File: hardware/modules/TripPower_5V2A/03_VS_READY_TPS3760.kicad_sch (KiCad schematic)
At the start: 13 parts, among them Q303 BVSS123LT1G 100V AEC-Q101, U302 TPS3760A012DYYRQ1

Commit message: feat(TripPower): replace leaking EN source follower with VS-only 300V automotive PNP/NPN gated high-side drive; isolate RUN and AUTO
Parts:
- removed D306: BAS70-02V-HG3-08 GATE TO RESET SCHOTTKY, Diode_SMD:D_SOD-523, symbol TripPower_Sym:BAS70_02V_A1_K2
- removed D307: SZMMSZ5240BT1G 10V GATE ZENER, Diode_SMD:D_SOD-123, symbol TripTracer_V1:PWR_DIODE
- removed D308: BAS70-02V-HG3-08 EN FAILSAFE CLAMP, Diode_SMD:D_SOD-523, symbol TripPower_Sym:BAS70_02V_A1_K2
- removed Q303: BVSS123LT1G 100V AEC-Q101, Package_TO_SOT_SMD:SOT-23, symbol TripPower_Sym:EN_PASS_NMOS_GSD
- removed R334: 470k 1% VS GATE DRIVE, Resistor_SMD:R_1206_3216Metric, symbol Tripmaster_Sym:R
- removed R335: 1M 1% GATE PULLDOWN, Resistor_SMD:R_1206_3216Metric, symbol Tripmaster_Sym:R
- added Q303: PMBTA92-Q 300V automotive, Package_TO_SOT_SMD:SOT-23, symbol TripPower_Sym:PNP_B1_E2_C3
- added Q304, Q305: PMBTA42-Q 300V automotive, Package_TO_SOT_SMD:SOT-23, symbol TripPower_Sym:NPN_B1_E2_C3
- added R336: 47k 1% PNP B-E OFF, Resistor_SMD:R_1206_3216Metric, symbol Tripmaster_Sym:R
- added R337: 220k 1% PNP BASE CURRENT, Resistor_SMD:R_1206_3216Metric, symbol Tripmaster_Sym:R
- added R339: 1M 1% RESET TO NPN READY BASE, Resistor_SMD:R_1206_3216Metric, symbol Tripmaster_Sym:R
- added R340: 1M 1% READY NPN BASE BLEED, Resistor_SMD:R_1206_3216Metric, symbol Tripmaster_Sym:R
- added R341: 100k 1% RUN NPN BASE BLEED, Resistor_SMD:R_1206_3216Metric, symbol Tripmaster_Sym:R
- R330: value 845k 1% VS-SENSE -> 825k 1% VS-SENSE, load compensated
- R332: value 1.91M 1% RESET FEEDBACK -> 1M 1% RESET FEEDBACK, loaded by NPN base
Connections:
- net GND: now also Q305.3 (C), R340.2, R341.2
- net VS_CLAMP: now also Q303.3 (C), R336.1
- net VS_READY_RESET_OD_PRELIM: now also R339.1
- new net PNP_BASE: Q303.1 (B), R336.2, R337.1
- new net PNP_OUT: Q303.2 (E)
- new net PNP_SINK: Q304.2 (E), R337.2
- new net READY_NPN_BASE: Q304.1 (B), R339.2, R340.1
- new net RUN_BASE: Q305.1 (B), R341.1
- new net RUN_BYPASS_NODE: Q304.3 (C), Q305.2 (E)
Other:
- note added: "REV2 PNP Q303 sourced ONLY from VS. U302 RESET HIGH drives Q304 NPN; AUTO R319 bridges Q305 RUN-NPN; RUN_CMD cannot feed EN directly. Old MOS gate/clamp removed. 9V and hot low-leakage remain unqualified."
- note removed: "Q303 series EN pass: AUTO R319 and RUN D305 feed EN_REQUEST_RAW (NO bypass); RESET asserted LOW drives D306 gate clamp and D308 EN clamp. Gate VS divider R334/R335; D307 10V gate Zener. C309 DNP. All cold/hot/leakage/surge gates OPEN."

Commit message: fix(TripPower): isolate USB RUN backfeed with automotive BAS116Q K3/A1/NC2 SOT23 diode in READY/RUN series sink
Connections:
- net RUN_BYPASS_NODE: no longer Q305.2 (E)
- new net RUN_SINK_C: Q305.2 (E)
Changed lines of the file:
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@@
 (global_label "RUN_BASE" (shape bidirectional) (at 284.48 264.16 0) (effects (font (size .9 .9)) (justify left)))
 (wire (pts (xy 320.04 259.08000000000004) (xy 325.12 259.08000000000004)) (stroke (width 0) (type default)))
-(global_label "RUN_BYPASS_NODE" (shape bidirectional) (at 325.12 259.08000000000004 0) (effects (font (size .9 .9)) (justify left)))
+(global_label "RUN_SINK_C" (shape bidirectional) (at 325.12 259.08000000000004 0) (effects (font (size .9 .9)) (justify left)))
 (wire (pts (xy 320.04 269.24) (xy 325.12 269.24)) (stroke (width 0) (type default)))
 (global_label "GND" (shape bidirectional) (at 325.12 269.24 0) (effects (font (size .9 .9)) (justify left)))

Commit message: fix(TripPower): correct KiCad mirrored screen-Y orientation BJT E2/C3 for Q303/Q304/Q305 native netlist
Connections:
- net GND: now also Q305.2 (E); no longer Q305.3 (C)
- net PNP_OUT: now also Q303.3 (C); no longer Q303.2 (E)
- net PNP_SINK: now also Q304.3 (C); no longer Q304.2 (E)
- net RUN_BYPASS_NODE: now also Q304.2 (E); no longer Q304.3 (C)
- net RUN_SINK_C: now also Q305.3 (C); no longer Q305.2 (E)
- net VS_CLAMP: now also Q303.2 (E); no longer Q303.3 (C)

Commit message: feat(TripPower): set R330 715k experimental 9V startup margin REV3 without changing 202V path
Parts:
- R330: value 825k 1% VS-SENSE, load compensated -> 715k 1% VS-SENSE REV3 12V START EXP; MPN MPN_PENDING -> CRCW1206715KFKEA
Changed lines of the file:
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@@
 (symbol (lib_id "Tripmaster_Sym:R") (at 74.93 137.16 0) (unit 1) (in_bom yes) (on_board yes) (dnp no)
 (property "Reference" "R330" (at 74.93 101.6 0) (effects (font (size 1 1))))
-(property "Value" "825k 1% VS-SENSE, load compensated" (at 74.93 102.87 0) (effects (font (size 1 1))))
+(property "Value" "715k 1% VS-SENSE REV3 12V START EXP" (at 74.93 102.87 0) (effects (font (size 1 1))))
 (property "Footprint" "Resistor_SMD:R_1206_3216Metric" (at 74.93 137.16 0) (effects (font (size 1 1)) (hide yes)))
-(property "MPN" "MPN_PENDING" (at 0 0 0) (effects (font (size 1 1)) (hide yes)))
+(property "MPN" "CRCW1206715KFKEA" (at 0 0 0) (effects (font (size 1 1)) (hide yes)))
 (pin "1")
 (pin "2")

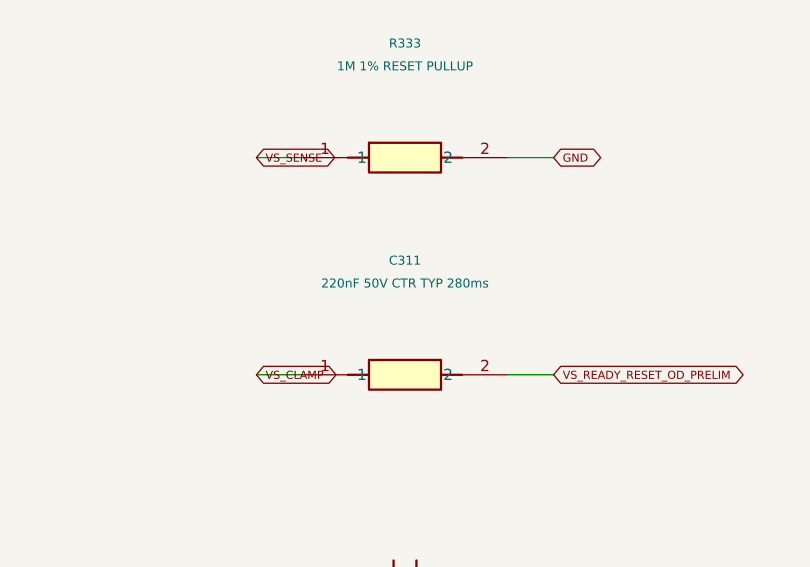
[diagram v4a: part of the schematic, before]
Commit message: feat(TripPower REV4): 330nF 100V automotive C311 increases reset startup delay margin
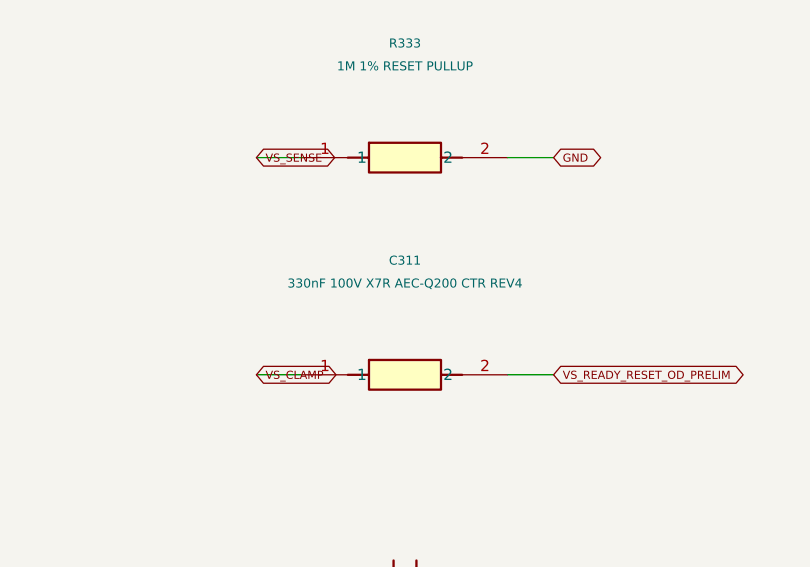
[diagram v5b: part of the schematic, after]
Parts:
- C311: value 220nF 50V CTR TYP 280ms -> 330nF 100V X7R AEC-Q200 CTR REV4; MPN MPN_PENDING -> C1206C334K1RACAUTO
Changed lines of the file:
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@@
 (symbol (lib_id "Tripmaster_Sym:C") (at 166.37 185.42 0) (unit 1) (in_bom yes) (on_board yes) (dnp no)
 (property "Reference" "C311" (at 166.37 148.59 0) (effects (font (size 1 1))))
-(property "Value" "220nF 50V CTR TYP 280ms" (at 166.37 151.13 0) (effects (font (size 1 1))))
+(property "Value" "330nF 100V X7R AEC-Q200 CTR REV4" (at 166.37 151.13 0) (effects (font (size 1 1))))
 (property "Footprint" "Capacitor_SMD:C_1206_3216Metric" (at 166.37 185.42 0) (effects (font (size 1 1)) (hide yes)))
-(property "MPN" "MPN_PENDING" (at 0 0 0) (effects (font (size 1 1)) (hide yes)))
+(property "MPN" "C1206C334K1RACAUTO" (at 0 0 0) (effects (font (size 1 1)) (hide yes)))
 (pin "1")
 (pin "2")

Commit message: bom(TripPower): lock C310 automotive 100nF 100V AEC-Q200 bypass
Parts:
- C310: MPN MPN_PENDING -> C1206C104K1RACAUTO; Supplier_URL (none) -> https://www.digikey.de/de/products/detail/kemet/C1206C104K1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
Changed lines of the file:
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@@
 (property "Value" "100nF 100V VDD BYPASS" (at 74.93 151.13 0) (effects (font (size 1 1))))
 (property "Footprint" "Capacitor_SMD:C_1206_3216Metric" (at 74.93 185.42 0) (effects (font (size 1 1)) (hide yes)))
-(property "MPN" "MPN_PENDING" (at 0 0 0) (effects (font (size 1 1)) (hide yes)))
-(pin "1")
+(property "MPN" "C1206C104K1RACAUTO" (at 0 0 0) (effects (font (size 1 1)) (hide yes)))
+(property "Supplier_URL" "https://www.digikey.de/de/products/detail/kemet/C1206C104K1RACAUTO/3314516" (at 0 0 0) (effects (font (size 1 1)) (hide yes))) (pin "1")
 (pin "2")
 (instances (project "TripPower_5V2A" (path "/f1512578-cc72-4c26-bf70-dbbd00000001/f1512578-cc72-4c26-bf70-dbbd00000005" (reference "C310") (unit 1)))))

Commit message: feat(TripPower REV5): replace U302/BJT control sheet with single TPS38 dual UV/open-drain supervisor and VS/RUN gating
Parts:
- removed Q303: PMBTA92-Q 300V automotive, Package_TO_SOT_SMD:SOT-23, symbol TripPower_Sym:PNP_B1_E2_C3
- removed Q304, Q305: PMBTA42-Q 300V automotive, Package_TO_SOT_SMD:SOT-23, symbol TripPower_Sym:NPN_B1_E2_C3
- removed R336: 47k 1% PNP B-E OFF, Resistor_SMD:R_1206_3216Metric, symbol Tripmaster_Sym:R
- removed R337: 220k 1% PNP BASE CURRENT, Resistor_SMD:R_1206_3216Metric, symbol Tripmaster_Sym:R
- removed R339: 1M 1% RESET TO NPN READY BASE, Resistor_SMD:R_1206_3216Metric, symbol Tripmaster_Sym:R
- removed R340: 1M 1% READY NPN BASE BLEED, Resistor_SMD:R_1206_3216Metric, symbol Tripmaster_Sym:R
- removed U302: TPS3760A012DYYRQ1, Tripmaster:TI_TPS3760_DYY14, symbol TripTracer_V1:TPS3760A012DYYRQ1
- added U302: TPS38A010122DSKRQ1, Tripmaster:TI_TPS38_DSK10, symbol TripPower_TPS38:TPS38A010122DSKRQ1
- C310: value 100nF 100V VDD BYPASS -> 100nF 100V TPS38 VDD BYPASS; Supplier_URL https://www.digikey.de/de/products/detail/kemet/C1206C104K1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 -> (none)
- C311: value 330nF 100V X7R AEC-Q200 CTR REV4 -> 330nF 100V X7R TPS38 CTR1
- R330: value 715k 1% VS-SENSE REV3 12V START EXP -> 715k 1% VS_READY VIN TOP
- R331: value 100k 1% SENSE-GND -> 100k 1% VS_READY SENSE GND; MPN MPN_PENDING -> RC1206FR-07100KL
- R332: value 1M 1% RESET FEEDBACK, loaded by NPN base -> 1M 1% CTRL_EN SCHMITT FEEDBACK; MPN MPN_PENDING -> RC1206FR-071ML
- R333: value 1M 1% RESET PULLUP -> 1M 1% VS_CLAMP CTRL_EN PULLUP; MPN MPN_PENDING -> RC1206FR-071ML
- R341: value 100k 1% RUN NPN BASE BLEED -> 1M 1% RUN_SENSE BLEED - RUN ONLY; MPN MPN_TBD -> RC1206FR-071ML
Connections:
- net CTR_READY: now also U302.6 (CTR1)
- net GND: now also U302.10 (GND)
- net VS_CLAMP: now also U302.1 (VDD)
- net VS_SENSE: now also U302.2 (SENSE1)
- net RUN_BASE renamed RUN_SENSE
- net RUN_SENSE: now also U302.3 (SENSE2)
- net VS_READY_RESET_OD_PRELIM renamed CTRL_EN
- net CTRL_EN: now also U302.4 (RESET1_N), U302.5 (RESET2_N)
- no-connect marks 1 -> 3
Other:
- note removed: "REV2 PNP Q303 sourced ONLY from VS. U302 RESET HIGH drives Q304 NPN; AUTO R319 bridges Q305 RUN-NPN; RUN_CMD cannot feed EN directly. Old MOS gate/clamp removed. 9V and hot low-leakage remain unqualified."
- title: TripPower VS_READY adjustable supervisor; AUTO/RUN via gated Q303 to CTRL_EN – prototype, not qualified -> TripPower REV5 TPS38-Q1 dual-UV VS_READY + RUN; guaranteed OD output levels; NOT vehicle released

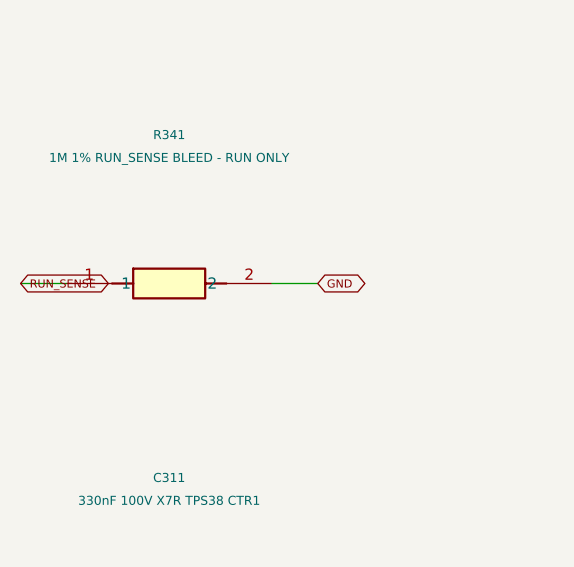
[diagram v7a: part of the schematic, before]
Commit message: feat(TripPower): DNP RUN-only R341 bleeder for minimal AUTO BOM
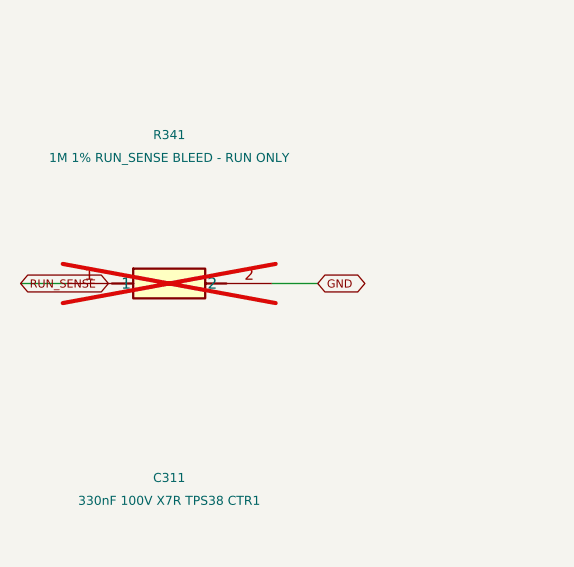
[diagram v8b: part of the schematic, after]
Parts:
- R341: now not fitted
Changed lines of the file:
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@@
 (wire (pts (xy 252.73 180.34) (xy 257.81 180.34)) (stroke (width 0) (type default)))
 (global_label "CTRL_EN" (shape bidirectional) (at 257.81 180.34 0) (effects (font (size 0.9 0.9)) (justify left)))
-(symbol (lib_id "Tripmaster_Sym:R") (at 88.9 218.44 0) (unit 1) (in_bom yes) (on_board yes) (dnp no)
+(symbol (lib_id "Tripmaster_Sym:R") (at 88.9 218.44 0) (unit 1) (in_bom yes) (on_board yes) (dnp yes)
 (property "Reference" "R341" (at 88.9 201.93 0) (effects (font (size 1 1))))
 (property "Value" "1M 1% RUN_SENSE BLEED - RUN ONLY" (at 88.9 204.47 0) (effects (font (size 1 1))))
